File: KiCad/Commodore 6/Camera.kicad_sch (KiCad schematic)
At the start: 19 parts, among them J5 FH12-24S-0.5SH_55_, J7 FH12-22S-0.5SH55

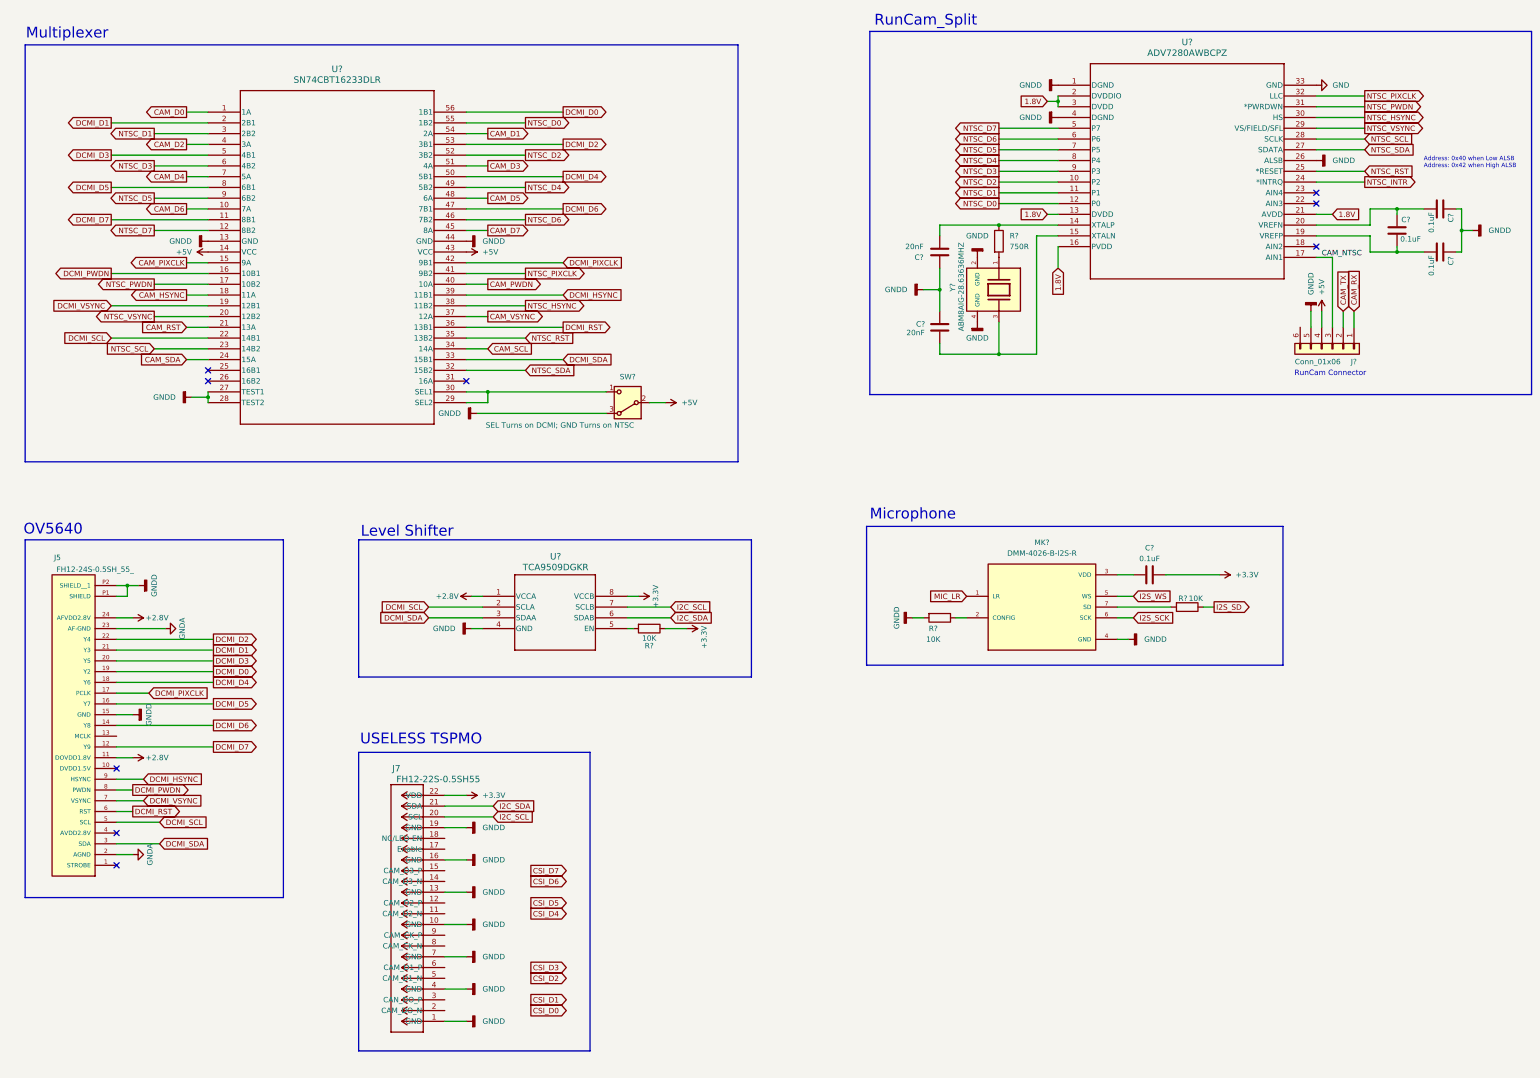
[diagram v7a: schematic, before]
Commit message: Adding Footprints
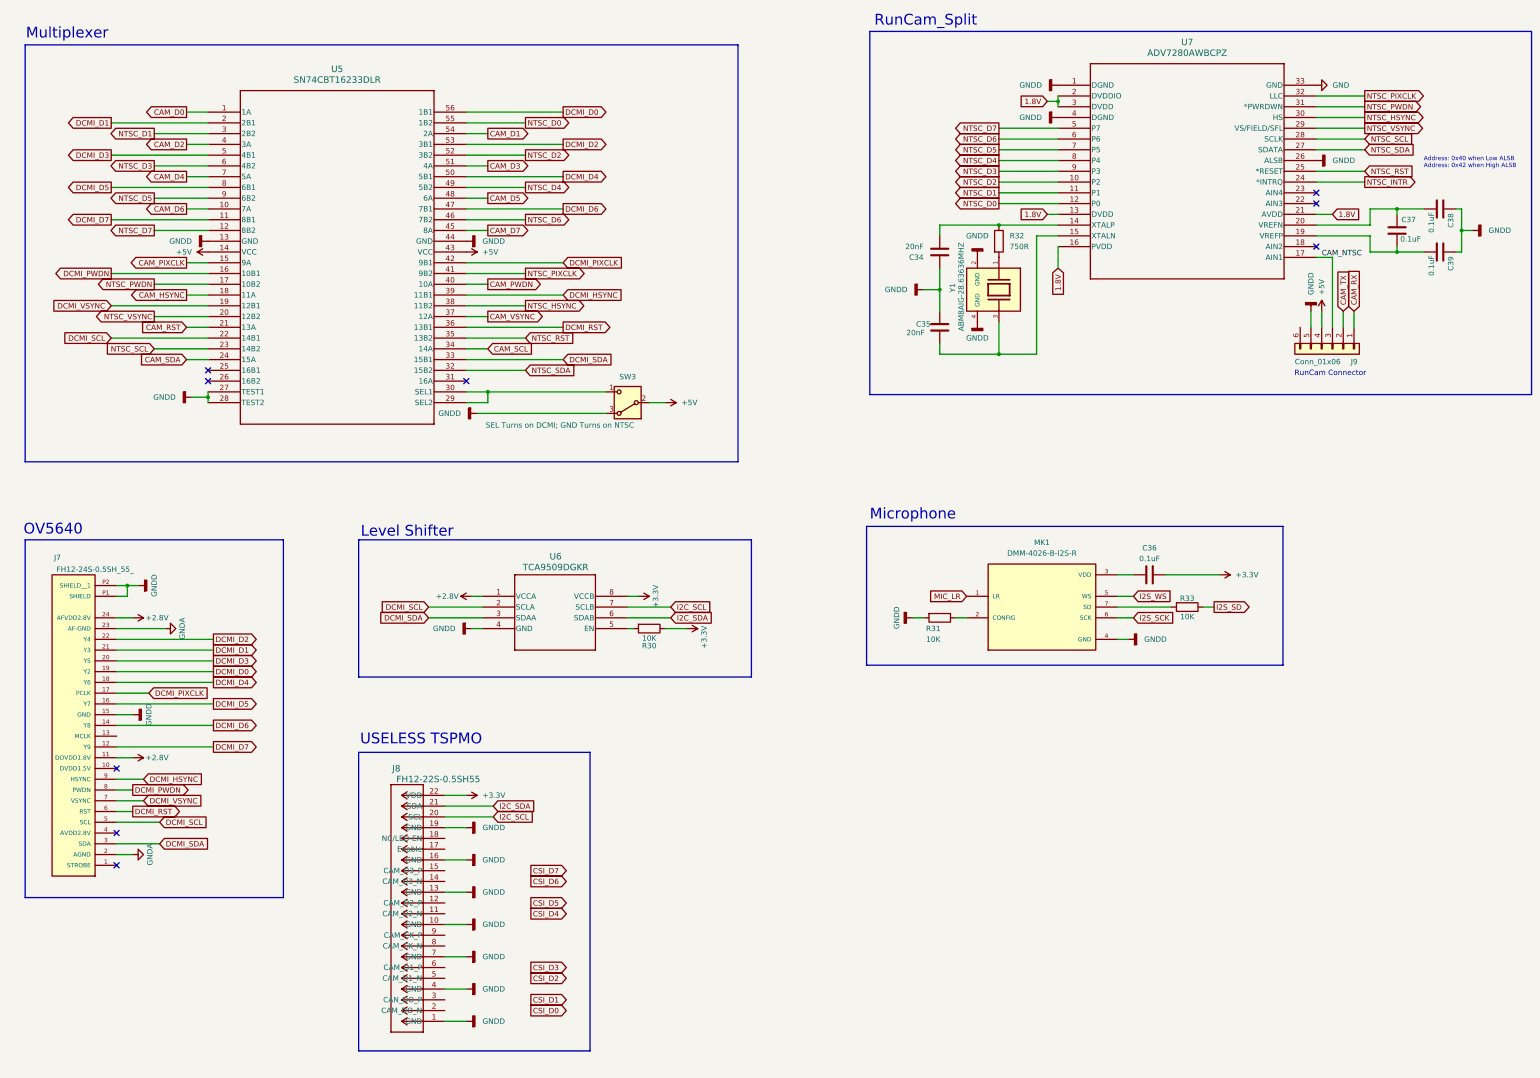
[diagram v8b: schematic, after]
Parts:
- C34, C35, C36, C37, C38, C39: renamed from C?; footprint (none) -> Capacitor_SMD:C_1206_3216Metric
- J8: renamed from J7; footprint CONN_FH12-22S-0.5SH55_HIR -> (none)
- R30, R31, R32, R33: renamed from R?; footprint (none) -> Resistor_SMD:R_1206_3216Metric
- U5: renamed from U?; footprint DL56 -> (none)
- U6: renamed from U?; footprint DGK8 -> (none)
- U7: renamed from U?; footprint CP-32-12_ADI -> (none)
- gave numbers to parts that had none: 4
- renumbered J5 to J7
